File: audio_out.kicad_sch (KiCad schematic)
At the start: 34 parts, among them SW2 Gain0, SW3 Gain1, U3 PAM8908JER, U4 PCM5102A, U8 AP7333-33SRG-7

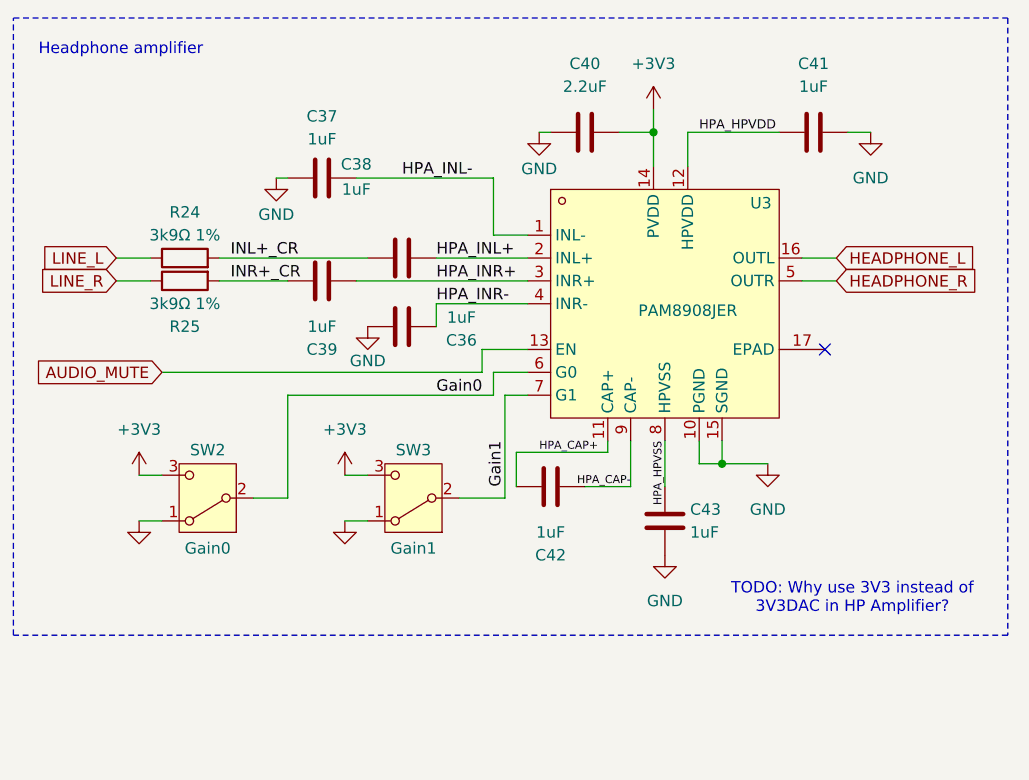
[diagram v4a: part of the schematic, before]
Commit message: Audio section is completely routed.
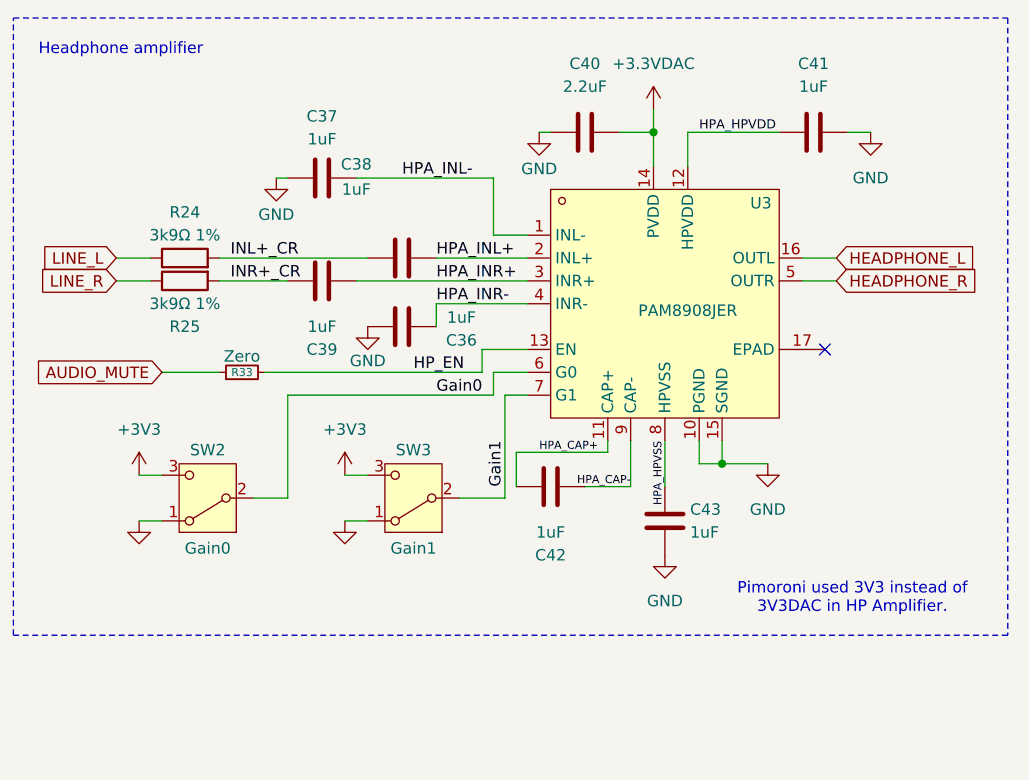
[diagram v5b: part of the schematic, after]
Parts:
- added R33: Zero, Resistor_SMD:R_1206_3216Metric, symbol Device:R_Small
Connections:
- net +3.3VDAC: now also C40.2, U3.14 (PVDD)
- net +3V3: no longer C40.2, U3.14 (PVDD)
- net AUDIO_MUTE: now also R33.1; no longer U3.13 (EN)
- new net HP_EN: R33.2, U3.13 (EN)
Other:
- note added: "Pimoroni used 3V3 instead of 3V3DAC in HP Amplifier."
- note removed: "TODO: Why use 3V3 instead of 3V3DAC in HP Amplifier?"
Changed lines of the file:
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@@
 	(wire
 		(pts
+			(xy 168.91 57.15) (xy 193.04 57.15)
+		)
+		(stroke
+			(width 0)
+			(type default)
+		)
+	)
+	(wire
+		(pts
 			(xy 104.14 38.1) (xy 123.19 38.1)
 		)
@@
 	(wire
 		(pts
-			(xy 157.48 57.15) (xy 193.04 57.15)
+			(xy 157.48 57.15) (xy 163.83 57.15)
 		)
 		(stroke
@@
 		)
 	)
-	(text "TODO: Why use 3V3 instead of\n3V3DAC in HP Amplifier?"
+	(text "Pimoroni used 3V3 instead of\n3V3DAC in HP Amplifier."
 		(exclude_from_sim no)
 		(at 234.188 82.296 0)
@@
 		)
 	)
+	(label "HP_EN"
+		(at 185.42 57.15 0)
+		(fields_autoplaced yes)
+		(effects
+			(font
+				(size 1.27 1.27)
+			)
+			(justify left bottom)
+		)
+	)
 	(label "DAC_CAPP"
 		(at 86.36 45.72 0)
@@
 			)
 		)
-		(property "Value" "+3V3"
+		(property "Value" "+3.3VDAC"
 			(at 212.09 22.86 0)
 			(effects
@@
 			)
 		)
+		(property "LCSC" ""
+			(at 212.09 27.94 0)
+			(effects
+				(font
+					(size 1.27 1.27)
+				)
+				(hide yes)
+			)
+		)
+		(property "DPFNOTES" ""
+			(at 212.09 27.94 0)
+			(effects
+				(font
+					(size 1.27 1.27)
+				)
+				(hide yes)
+			)
+		)
+		(property "DPFURL" ""
+			(at 212.09 27.94 0)
+			(effects
+				(font
+					(size 1.27 1.27)
+				)
+				(hide yes)
+			)
+		)
 		(pin "1"
 		)
@@
 					(unit 1)
 				)
+			)
+		)
+	)
+	(symbol
+		(lib_id "Device:R_Small")
+		(at 166.37 57.15 90)
+		(unit 1)
+		(exclude_from_sim no)
+		(in_bom yes)
+		(on_board yes)
+		(dnp no)
+		(property "Reference" "R33"
+			(at 166.37 57.15 90)
+			(effects
+				(font
+					(size 0.889 0.889)
+				)
+			)
+		)
+		(property "Value" "Zero"
+			(at 166.37 55.372 90)
+			(effects
+				(font
+					(size 1.27 1.27)
+				)
+			)
+		)
+		(property "Footprint" "Resistor_SMD:R_1206_3216Metric"
+			(at 166.37 57.15 0)
+			(effects
+				(font
+					(size 1.27 1.27)
+				)
+				(hide yes)
+			)
+		)
+		(property "Datasheet" "~"
+			(at 166.37 57.15 0)
+			(effects
+				(font
+					(size 1.27 1.27)
+				)
+				(hide yes)
+			)
+		)
+		(property "Description" "Resistor, small symbol"
+			(at 166.37 57.15 0)
+			(effects
+				(font
+					(size 1.27 1.27)
+				)
+				(hide yes)
+			)
+		)
+		(property "LCSC" ""
+			(at 166.37 57.15 0)
+			(effects
+				(font
+					(size 1.27 1.27)
+				)
+				(hide yes)
+			)
+		)
+		(property "DPFNOTES" "For Routing"
+			(at 166.37 57.15 0)
+			(effects
+				(font
+					(size 1.27 1.27)
+				)
+				(hide yes)
+			)
+		)
+		(property "DPFURL" ""
+			(at 166.37 57.15 0)
+			(effects
+				(font
+					(size 1.27 1.27)
+				)
+				(hide yes)
+			)
+		)
+		(pin "1"
+		)
+		(pin "2"
+		)
+		(instances
+			(project "stm-midi-poc1"
+				(path "/7cd74113-1f92-4dcc-8610-19aa9fc81e5f/c9577070-7433-48cd-ae0f-c607bda27147"
+					(reference "R33")
+					(unit 1)
+				)

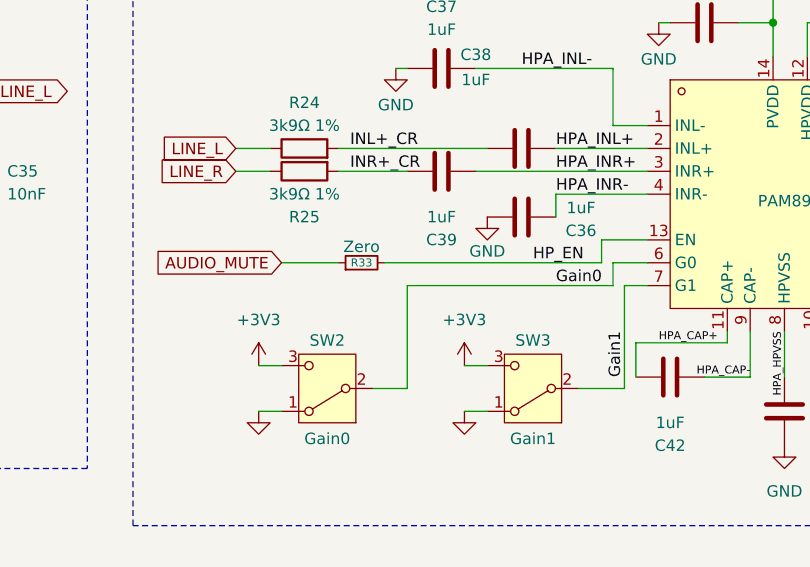
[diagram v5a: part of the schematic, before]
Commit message: Start routing through the new signal layer.
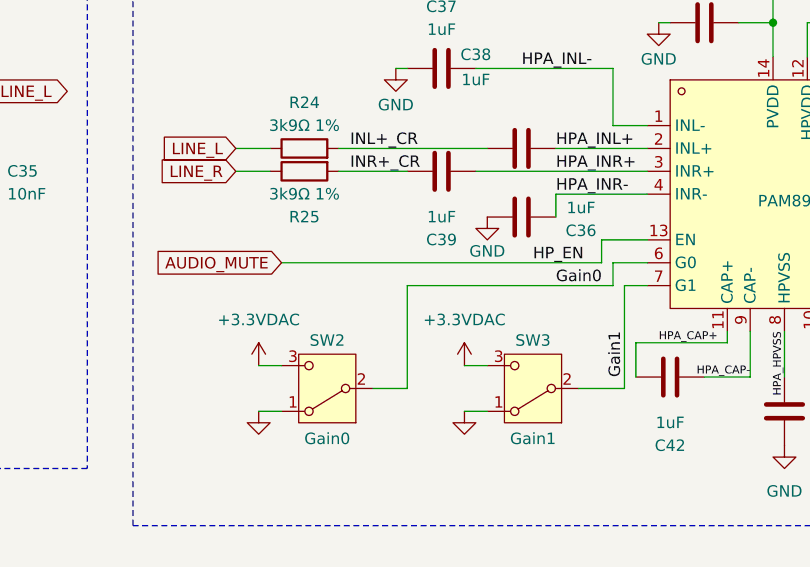
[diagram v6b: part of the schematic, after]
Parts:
- removed R33: Zero, Resistor_SMD:R_1206_3216Metric, symbol Device:R_Small
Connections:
- net HP_EN is gone; now on net AUDIO_MUTE: U3.13 (EN)
- net +3.3VDAC: now also SW2.3 (C), SW3.3 (C)
- net +3V3: no longer SW2.3 (C), SW3.3 (C)
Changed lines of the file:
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@@
 	(wire
 		(pts
-			(xy 168.91 57.15) (xy 193.04 57.15)
-		)
-		(stroke
-			(width 0)
-			(type default)
-		)
-	)
-	(wire
-		(pts
 			(xy 104.14 38.1) (xy 123.19 38.1)
 		)
@@
 	(wire
 		(pts
-			(xy 157.48 57.15) (xy 163.83 57.15)
+			(xy 157.48 57.15) (xy 193.04 57.15)
 		)
 		(stroke
@@
 	)
 	(symbol
-		(lib_id "Device:R_Small")
-		(at 166.37 57.15 90)
+		(lib_id "power:+3V3")
+		(at 154.94 68.58 0)
 		(unit 1)
 		(exclude_from_sim no)
@@
 		(on_board yes)
 		(dnp no)
-		(property "Reference" "R33"
-			(at 166.37 57.15 90)
-			(effects
-				(font
-					(size 0.889 0.889)
-				)
-			)
-		)
-		(property "Value" "Zero"
-			(at 166.37 55.372 90)
-			(effects
-				(font
-					(size 1.27 1.27)
-				)
-			)
-		)
-		(property "Footprint" "Resistor_SMD:R_1206_3216Metric"
-			(at 166.37 57.15 0)
-			(effects
-				(font
-					(size 1.27 1.27)
-				)
-				(hide yes)
-			)
-		)
-		(property "Datasheet" "~"
-			(at 166.37 57.15 0)
-			(effects
-				(font
-					(size 1.27 1.27)
-				)
-				(hide yes)
-			)
-		)
-		(property "Description" "Resistor, small symbol"
-			(at 166.37 57.15 0)
+		(fields_autoplaced yes)
+		(property "Reference" "#PWR067"
+			(at 154.94 72.39 0)
 			(effects
 				(font
@@
 			)
 		)
-		(property "LCSC" ""
-			(at 166.37 57.15 0)
+		(property "Value" "+3.3VDAC"
+			(at 154.94 63.5 0)
 			(effects
 				(font
 					(size 1.27 1.27)
 				)
-				(hide yes)
 			)
 		)
-		(property "DPFNOTES" "For Routing"
-			(at 166.37 57.15 0)
+		(property "Footprint" ""
+			(at 154.94 68.58 0)
 			(effects
 				(font
@@
 			)
 		)
-		(property "DPFURL" ""
-			(at 166.37 57.15 0)
+		(property "Datasheet" ""
+			(at 154.94 68.58 0)
 			(effects
 				(font
@@
 			)
 		)
-		(pin "1"
-		)
-		(pin "2"
-		)
-		(instances
-			(project "stm-midi-poc1"
-				(path "/7cd74113-1f92-4dcc-8610-19aa9fc81e5f/c9577070-7433-48cd-ae0f-c607bda27147"
-					(reference "R33")
-					(unit 1)
-				)
-			)
-		)
-	)
-	(symbol
-		(lib_id "power:+3V3")
-		(at 154.94 68.58 0)
-		(unit 1)
-		(exclude_from_sim no)
-		(in_bom yes)
-		(on_board yes)
-		(dnp no)
-		(fields_autoplaced yes)
-		(property "Reference" "#PWR067"
-			(at 154.94 72.39 0)
+		(property "Description" "Power symbol creates a global label with name \"+3V3\""
+			(at 154.94 68.58 0)
 			(effects
 				(font
@@
 			)
 		)
-		(property "Value" "+3V3"
-			(at 154.94 63.5 0)
-			(effects
-				(font
-					(size 1.27 1.27)
-				)
-			)
-		)
-		(property "Footprint" ""
+		(property "LCSC" ""
 			(at 154.94 68.58 0)
 			(effects
@@
 			)
 		)
-		(property "Datasheet" ""
+		(property "DPFNOTES" ""
 			(at 154.94 68.58 0)
 			(effects
@@
 			)
 		)
-		(property "Description" "Power symbol creates a global label with name \"+3V3\""
+		(property "DPFURL" ""
 			(at 154.94 68.58 0)
 			(effects
@@
 			)
 		)
-		(property "Value" "+3V3"
+		(property "Value" "+3.3VDAC"
 			(at 177.8 63.5 0)
 			(effects
@@
 			(at 177.8 68.58 0)
 			(effects
+				(font
+					(size 1.27 1.27)
+				)
+				(hide yes)
+			)
+		)
+		(property "LCSC" ""
+			(at 177.8 68.58 0)
+			(effects
+				(font
+					(size 1.27 1.27)
+				)
+				(hide yes)
+			)
+		)
+		(property "DPFNOTES" ""
+			(at 177.8 68.58 0)
+			(effects
+				(font
+					(size 1.27 1.27)
+				)
+				(hide yes)
+			)
+		)
+		(property "DPFURL" ""
+			(at 177.8 68.58 0)
+			(effects

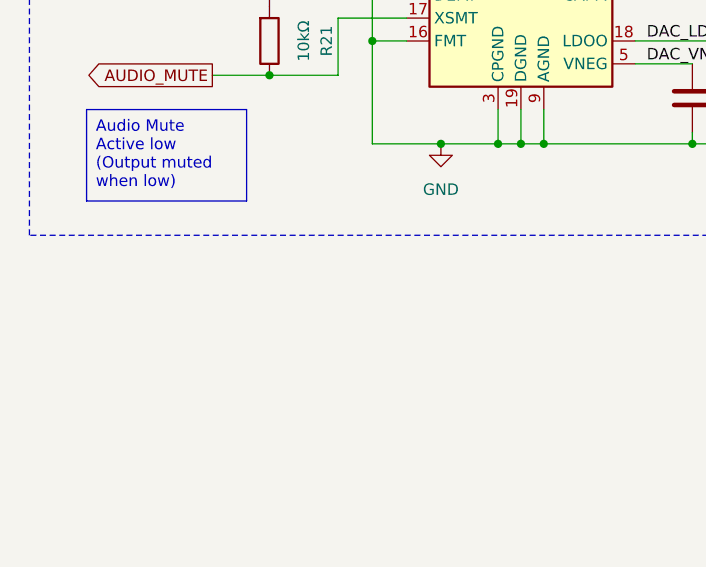
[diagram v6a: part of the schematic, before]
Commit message: All power now routed. TODO: Fix all DRC warnings
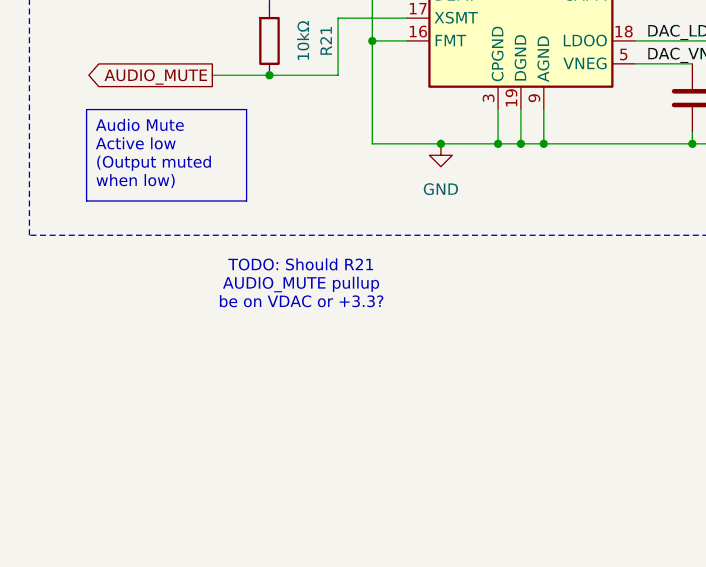
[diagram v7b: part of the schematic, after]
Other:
- note added: "TODO: Should R21 AUDIO_MUTE pullup be on VDAC or +3.3?"
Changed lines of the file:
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@@
+		)
+	)
+	(text "TODO: Should R21\nAUDIO_MUTE pullup\nbe on VDAC or +3.3?"
+		(exclude_from_sim no)
+		(at 48.006 85.598 0)
+		(effects
+			(font
+				(size 1.27 1.27)
+			)
 		)
 	)

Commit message: 1. Update README with info on my KiCAD component library. 2. Add Fiducial markers. 3. Add LCSC IDs for all parts in BOM.
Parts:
- C23, C24, C40: LCSC (none) -> C377773
- R21: DPFNOTES (none) -> UNI-ROYAL(Uniroyal Elec) 0402WGF1002TCE 62.5mW Thick Film R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; LCSC (none) -> C25744
- R22, R23: DPFNOTES (none) -> 62.5mW Thick Film Resistors 50V ±100ppm/℃ ±1% 220Ω 0402 Chi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; LCSC (none) -> C25091
- R24, R25: DPFNOTES (none) -> 62.5mW Thick Film Resistors 50V ±100ppm/℃ ±1% 3.9kΩ 0402 Ch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; LCSC (none) -> C51721
- U3: LCSC (none) -> C33233
- U8: LCSC (none) -> C150745
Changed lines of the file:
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@@
 			)
 		)
-		(property "Datasheet" "~"
+		(property "Datasheet" "https://www.lcsc.com/datasheet/lcsc_datasheet_2206010000_UNI-ROYAL-Uniroyal-Elec-0402WGF3901TCE_C51721.pdf"
 			(at 160.02 46.99 0)
 			(effects
@@
 			)
 		)
-		(property "LCSC" ""
+		(property "LCSC" "C51721"
 			(at 160.02 46.99 0)
 			(effects
@@
 			)
 		)
-		(property "DPFNOTES" ""
+		(property "DPFNOTES" "62.5mW Thick Film Resistors 50V ±100ppm/℃ ±1% 3.9kΩ 0402 Chip Resistor - Surface Mount ROHS"
 			(at 160.02 46.99 0)
 			(effects
@@
 			)
 		)
-		(property "Datasheet" "~"
+		(property "Datasheet" "https://www.lcsc.com/datasheet/lcsc_datasheet_2206010000_UNI-ROYAL-Uniroyal-Elec-0402WGF3901TCE_C51721.pdf"
 			(at 160.02 44.45 0)
 			(effects
@@
 			)
 		)
-		(property "LCSC" ""
+		(property "LCSC" "C51721"
 			(at 160.02 44.45 0)
 			(effects
@@
 			)
 		)
-		(property "DPFNOTES" ""
+		(property "DPFNOTES" "62.5mW Thick Film Resistors 50V ±100ppm/℃ ±1% 3.9kΩ 0402 Chip Resistor - Surface Mount ROHS"
 			(at 160.02 44.45 0)
 			(effects
@@
 			)
 		)
-		(property "Datasheet" "~"
+		(property "Datasheet" "https://www.lcsc.com/datasheet/lcsc_datasheet_2206010100_UNI-ROYAL-Uniroyal-Elec-0402WGF1002TCE_C25744.pdf"
 			(at 44.45 58.42 0)
 			(effects
@@
 			)
 		)
-		(property "LCSC" ""
+		(property "LCSC" "C25744"
 			(at 44.45 58.42 0)
 			(effects
@@
 			)
 		)
-		(property "DPFNOTES" ""
+		(property "DPFNOTES" "UNI-ROYAL(Uniroyal Elec) 0402WGF1002TCE 62.5mW Thick Film Resistors 50V ±100ppm/℃ ±1% 10kΩ 0402 Chip Resistor "
 			(at 44.45 58.42 0)
 			(effects
@@
 			)
 		)
-		(property "Datasheet" "~"
+		(property "Datasheet" "https://www.lcsc.com/datasheet/lcsc_datasheet_2304140030_YAGEO-CC0805KRX7R9BB104_C49678.pdf"
 			(at 91.44 64.77 0)
 			(effects
@@
 			)
 		)
-		(property "LCSC" ""
+		(property "LCSC" "C377773"
 			(at 91.44 64.77 0)
 			(effects
@@
 			)
 		)
+		(property "LCSC" "C150745"
+			(at 38.1 184.15 0)
+			(effects
+				(font
+					(size 1.27 1.27)
+				)
+				(hide yes)
+			)
+		)
 		(pin "2"
 		)
@@
 			)
 		)
-		(property "Datasheet" "~"
+		(property "Datasheet" "https://www.lcsc.com/datasheet/lcsc_datasheet_2304140030_YAGEO-CC0805KRX7R9BB104_C49678.pdf"
 			(at 88.9 49.53 0)
 			(effects
@@
 			)
 		)
-		(property "LCSC" ""
+		(property "LCSC" "C377773"
 			(at 88.9 49.53 0)
 			(effects
@@
 			)
 		)
-		(property "Datasheet" "~"
+		(property "Datasheet" "https://www.lcsc.com/datasheet/lcsc_datasheet_1808041445_ALPSALPINE-SSSS811101_C109335.pdf"
 			(at 185.42 63.5 0)
 			(effects
@@
 			)
 		)
-		(property "Datasheet" "~"
+		(property "Datasheet" "https://www.lcsc.com/datasheet/lcsc_datasheet_2304140030_YAGEO-CC0805KRX7R9BB104_C49678.pdf"
 			(at 204.47 30.48 0)
 			(effects
@@
 			)
 		)
-		(property "LCSC" ""
+		(property "LCSC" "C377773"
 			(at 204.47 30.48 0)
 			(effects
@@
 			)
 		)
-		(property "Datasheet" "~"
+		(property "Datasheet" "https://www.lcsc.com/datasheet/lcsc_datasheet_2205311900_UNI-ROYAL-Uniroyal-Elec-0402WGF2200TCE_C25091.pdf"
 			(at 100.33 38.1 0)
 			(effects
@@
 			)
 		)
-		(property "LCSC" ""
+		(property "LCSC" "C25091"
 			(at 100.33 38.1 0)
 			(effects
@@
 			)
 		)
-		(property "DPFNOTES" ""
+		(property "DPFNOTES" "62.5mW Thick Film Resistors 50V ±100ppm/℃ ±1% 220Ω 0402 Chip Resistor - Surface Mount ROHS"
 			(at 100.33 38.1 0)
 			(effects
@@
 			)
 		)
-		(property "LCSC" ""
+		(property "LCSC" "C33233"
 			(at 213.36 46.99 0)
 			(effects
@@
 			)
 		)
-		(property "Datasheet" "~"
+		(property "Datasheet" "https://www.lcsc.com/datasheet/lcsc_datasheet_2205311900_UNI-ROYAL-Uniroyal-Elec-0402WGF2200TCE_C25091.pdf"
 			(at 100.33 40.64 0)
 			(effects
@@
 			)
 		)
-		(property "LCSC" ""
+		(property "LCSC" "C25091"
 			(at 100.33 40.64 0)
 			(effects
@@
 			)
 		)
-		(property "DPFNOTES" ""
+		(property "DPFNOTES" "62.5mW Thick Film Resistors 50V ±100ppm/℃ ±1% 220Ω 0402 Chip Resistor - Surface Mount ROHS"
 			(at 100.33 40.64 0)
 			(effects
@@
 			)
 		)
-		(property "Datasheet" "~"
+		(property "Datasheet" "https://www.lcsc.com/datasheet/lcsc_datasheet_1808041445_ALPSALPINE-SSSS811101_C109335.pdf"
 			(at 162.56 63.5 0)
 			(effects
